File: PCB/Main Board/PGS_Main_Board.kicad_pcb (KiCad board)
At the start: 4 copper layers, 109.9 x 60.8 mm, 132 parts, among them J1 SM02B-SURS-TF_LF__SN_, J2 SM02B-SURS-TF_LF__SN_, J3 Molex 505110-0892, J5 Molex 505110-0892, J6 Molex 505110-0492, J7 Molex 505110-0492, J8 Conn_01x04_Pin, J9 Molex 505110-1792, Q1 MMBT2222A, Q2 MMBT2222A, SW1 TS-1187A-C-A-B, SW10 SW_Push, SW11 SW_Push, SW12 SW_Push, SW13 SW_Push, SW14 EVQ-P0E07K, SW15 1TS026A-1000-0550, SW16 TS-1187A-C-A-B, SW2 TS-1187A-C-A-B, SW3 TS-1187A-C-A-B, SW4 TS-1187A-C-A-B, SW5 SW_Push, SW6 SW_Push, SW7 SW_Push, SW8 SW_Push, SW9 EVQ-P0E07K, U1 RP2040, U2 TPS630001RCR, U3 GD25Q80EEIGR, U4 ST_LSM6, U5 ST_LSM6, Y1 ABM8-272-T3

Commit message: PCB Routing
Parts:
- C1, C15, C16, C17, C2, C20, C24, C25, C26, C27, C4, C5, R1, R11, S1, U2, Y1: moved to B.Cu
- moved R11 94.8 mm to (65.5, 39.7), turned to 45 degrees
- moved C16 90.2 mm to (65.5, 38.3), turned to -135 degrees
- moved C4 86.5 mm to (68.8, 32.6), turned to -135 degrees
- moved D13 85.7 mm to (56.6, 43.4)
- moved D14 84.7 mm to (56.6, 46.2)
- moved C5 84.1 mm to (65.3, 30.8), turned to -135 degrees
- moved R1 78.4 mm to (68.0, 22.2), turned to 45 degrees
- moved C24 76.7 mm to (57.0, 14.9), turned to 180 degrees
- moved C26 73.3 mm to (58.5, 14.9)
- moved R24 72.3 mm to (105.4, 30.2)
- moved D15 72.2 mm to (92.3, 38.1), turned to 180 degrees
- moved C20 67.7 mm to (68.9, 20.8), turned to -45 degrees
- moved S1 66.2 mm to (76.6, 22.7), turned to 180 degrees
- moved D16 65.4 mm to (92.3, 35.3), turned to 180 degrees
- moved C27 60.3 mm to (84.1, 14.9)
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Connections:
- net Net-(U1-USB_DM) renamed DI-
- net Net-(U1-USB_DP) renamed DI+
- J9 pad 13: D+ -> VBUS_SYS
- J9 pad 14: D- -> VBUS_SYS
- J9 pad 15: VBUS_SYS -> D+
- J9 pad 16: VBUS_SYS -> D-
- R21 pad 1: Net-(U1-GPIO16) -> unconnected-(R21-Pad1)
- R22 pad 1: Net-(U1-GPIO17) -> unconnected-(R22-Pad1)
- R24 pad 1: Net-(U1-GPIO19) -> Net-(U1-GPIO25)
- SW10 pad 2: Net-(D15A-A) -> Net-(D16B-A)
- SW11 pad 2: Net-(D15B-A) -> Net-(D16A-A)
- SW12 pad 2: Net-(D15C-A) -> Net-(D15A-A)
- SW13 pad 2: Net-(D16A-A) -> Net-(D15B-A)
- SW5 pad 2: Net-(D13A-A) -> Net-(D14A-A)
- SW6 pad 2: Net-(D13B-A) -> Net-(D13C-A)
- SW7 pad 2: Net-(D13C-A) -> Net-(D14B-A)
- SW8 pad 2: Net-(D14A-A) -> Net-(D13B-A)
- U1 pad 27: Net-(U1-GPIO16) -> I2C0_SDA
- U1 pad 28: Net-(U1-GPIO17) -> I2C0_SCL
- U1 pad 30: Net-(U1-GPIO19) -> unconnected-(U1-GPIO19-Pad30)
- U1 pad 31: ADC_ADDR_0 -> unconnected-(U1-GPIO20-Pad31)
- U1 pad 32: ADC_ADDR_1 -> unconnected-(U1-GPIO21-Pad32)
- U1 pad 36: I2C0_SDA -> unconnected-(U1-GPIO24-Pad36)
- U1 pad 37: I2C0_SCL -> Net-(U1-GPIO25)
- U1 pad 38: unconnected-(U1-GPIO26_ADC0-Pad38) -> ADC_ADDR_0
- U1 pad 39: unconnected-(U1-GPIO27_ADC1-Pad39) -> ADC_ADDR_1
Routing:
- net +3V3: track 0.00 -> 74.5 mm, vias 0 -> 31
- net GND: track 0.00 -> 65.3 mm, vias 0 -> 24
- net Net-(D15C-A): track 0.00 -> 53.9 mm, vias 0 -> 1
- net Net-(D13B-A): track 0.00 -> 53.6 mm
- net Net-(RGB3-DOUT): track 0.00 -> 47.8 mm
- net Net-(D16A-A): track 0.00 -> 41.1 mm, vias 0 -> 1
- net Net-(D13A-A): track 0.00 -> 38.7 mm
- net I2C0_SDA: track 0.00 -> 35.8 mm, vias 0 -> 3
- net BAT_LVL: track 0.00 -> 35.1 mm
- net I2C0_SCL: track 0.00 -> 34.4 mm, vias 0 -> 3
- net Net-(RGB5-DOUT): track 0.00 -> 33.6 mm
- net Net-(D15B-A): track 0.00 -> 31.9 mm, vias 0 -> 1
- net WL_CS: track 0.00 -> 29.7 mm
- net WL_CLK: track 0.00 -> 28.9 mm
- net I2C1_SCL: track 0.00 -> 28.6 mm, vias 0 -> 1
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
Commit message: Routing update
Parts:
- removed C15, C17: 10uF, Capacitor_SMD:C_0805_2012Metric
- removed C16: 100nF, Capacitor_SMD:C_0201_0603Metric
- removed D7: CUS08F30,H3F, Diode_SMD:D_SOD-323_HandSoldering
- removed L1: 1.3A 2.2uH ±20% 80mΩ, Inductor_SMD:L_1008_2520Metric
- removed R23: 100R, Resistor_SMD:R_0201_0603Metric
- removed TP1, TP2, TP3, TP4: TestPoint, TestPoint:TestPoint_Pad_2.0x2.0mm
- removed TP5: TestPoint, TestPoint:TestPoint_Pad_D1.5mm
- removed U2: TPS630001RCR, hhl:VREG_V62_16624-01YE
- R18, R19, R20, R21, R22: moved to B.Cu
- moved R9 138.3 mm to (28.1, 66.2), turned to 180 degrees
- moved T1 135.2 mm to (26.9, 58.1), turned to -90 degrees
- moved T2 134.0 mm to (24.8, 58.1), turned to -90 degrees
- moved C12 131.4 mm to (32.7, 63.7)
- moved C11 124.6 mm to (27.9, 68.5)
- moved R5 120.3 mm to (32.6, 58.1)
- moved C13 118.0 mm to (115.7, 65.2), turned to 90 degrees
- moved R10 117.8 mm to (113.1, 66.2)
- moved R7 117.1 mm to (33.8, 58.6), turned to -90 degrees
- moved C9 116.9 mm to (32.6, 58.9), turned to 180 degrees
- moved C14 113.5 mm to (109.7, 63.4), turned to 180 degrees
- moved T3 103.7 mm to (118.9, 58.4)
- moved T4 102.7 mm to (118.9, 60.5)
- moved Q1 100.1 mm to (32.8, 61.3), turned to -90 degrees
- moved R6 99.9 mm to (112.6, 56.6), turned to 90 degrees
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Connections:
- D11 pad 2: Net-(D11B-A) -> T_ZR_OUT
- D12 pad 1: T_ZR_OUT -> Net-(D12A-A)
- D8 pad 2: Net-(D8B-A) -> T_ZL_OUT
- D8 pad 5: B -> D
- D8 pad 6: A -> E
- D9 pad 1: T_ZL_OUT -> STICK_L_BTN_OUT
- D9 pad 2: STICK_L_BTN_OUT -> Net-(D9B-A)
- D9 pad 5: E -> A
- D9 pad 6: D -> B
- J3 pad 7: G -> F
- J5 pad 7: F -> G
- J6 pad 1: F -> G
- J6 pad 4: F -> G
- J7 pad 1: G -> F
- J7 pad 4: G -> F
- J9 pad 13: VBUS_SYS -> +3V3
- J9 pad 14: VBUS_SYS -> +3V3
- R11 pad 1: VBUS_SYS -> Net-(U1-GPIO10)
- R11 pad 2: Net-(U2-EN) -> A
- R15 pad 1: Net-(U1-GPIO10) -> unconnected-(R15-Pad1)
- R16 pad 1: Net-(U1-GPIO11) -> unconnected-(R16-Pad1)
- R17 pad 1: Net-(U1-GPIO12) -> unconnected-(R17-Pad1)
- R18 pad 1: Net-(U1-GPIO13) -> Net-(U1-GPIO15)
- R20 pad 1: Net-(U1-GPIO15) -> Net-(U1-GPIO13)
- R21 pad 1: unconnected-(R21-Pad1) -> Net-(U1-GPIO12)
- R22 pad 1: unconnected-(R22-Pad1) -> Net-(U1-GPIO11)
- S1 pad 2: LY -> STICK_R_X_OUT
- S1 pad 4: LX -> STICK_R_Y_OUT
- S1 pad 7: RX -> STICK_L_X_OUT
- S1 pad 9: RY -> STICK_L_Y_OUT
- SW1 pad A: F -> G
- SW1 pad B: F -> G
- SW2 pad A: F -> G
- SW2 pad B: F -> G
- SW2 pad C: Net-(D8B-A) -> Net-(D9B-A)
- SW2 pad D: Net-(D8B-A) -> Net-(D9B-A)
- SW3 pad A: G -> F
- SW3 pad B: G -> F
- SW4 pad A: G -> F
- SW4 pad B: G -> F
- SW4 pad C: Net-(D11B-A) -> Net-(D12A-A)
- SW4 pad D: Net-(D11B-A) -> Net-(D12A-A)
- U1 pad 29: Net-(U1-GPIO18) -> unconnected-(U1-GPIO18-Pad29)
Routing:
- net F: track 0.00 -> 109.0 mm, vias 0 -> 5
- net H: track 0.00 -> 82.5 mm, vias 0 -> 8
- net STICK_L_Y_OUT: track 0.00 -> 52.6 mm, vias 0 -> 2
- net STICK_L_X_OUT: track 0.00 -> 51.7 mm, vias 0 -> 2
- net D: track 0.00 -> 35.2 mm, vias 0 -> 2
- net E: track 0.00 -> 34.9 mm, vias 0 -> 2
- net C: track 0.00 -> 32.9 mm, vias 0 -> 2
- net B: track 0.00 -> 32.2 mm, vias 0 -> 2
- net A: track 0.00 -> 29.0 mm, vias 0 -> 2
- net LRA_R+: track 0.00 -> 22.5 mm, vias 0 -> 1
- net STICK_R_BTN_OUT: track 0.00 -> 21.7 mm, vias 0 -> 1
- net VBUS_SYS: track 20.3 -> 0.00 mm
- net LRA_L+: track 0.00 -> 19.9 mm, vias 0 -> 1
- net LRA_R-: track 0.00 -> 18.5 mm, vias 0 -> 1
- net STICK_L_BTN_OUT: track 0.00 -> 17.1 mm, vias 0 -> 1
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
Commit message: More Routing
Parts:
- C21, R15, R16, R17: moved to B.Cu
- moved R15 67.3 mm to (72.2, 19.7), turned to 45 degrees
- moved R17 66.1 mm to (73.6, 22.5), turned to 90 degrees
- moved R16 65.4 mm to (71.6, 19.1), turned to 45 degrees
- moved C21 65.0 mm to (72.9, 21.2), turned to -45 degrees
- moved R24 1.63 mm to (105.3, 28.6)
- moved D11 0.34 mm to (84.5, 31.8)
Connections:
- J3 pad 7: F -> G
- J5 pad 7: G -> F
- J6 pad 1: G -> F
- J6 pad 4: G -> F
- J7 pad 1: F -> G
- J7 pad 4: F -> G
- R15 pad 1: unconnected-(R15-Pad1) -> Net-(U1-GPIO19)
- R16 pad 1: unconnected-(R16-Pad1) -> Net-(U1-GPIO18)
- R17 pad 1: unconnected-(R17-Pad1) -> Net-(U1-GPIO22)
- S1 pad 2: STICK_R_X_OUT -> STICK_R_Y_OUT
- S1 pad 4: STICK_R_Y_OUT -> STICK_R_X_OUT
- SW1 pad A: G -> F
- SW1 pad B: G -> F
- SW2 pad A: G -> F
- SW2 pad B: G -> F
- SW3 pad A: F -> G
- SW3 pad B: F -> G
- SW4 pad A: F -> G
- SW4 pad B: F -> G
- U1 pad 29: unconnected-(U1-GPIO18-Pad29) -> Net-(U1-GPIO18)
- U1 pad 30: unconnected-(U1-GPIO19-Pad30) -> Net-(U1-GPIO19)
- U1 pad 31: unconnected-(U1-GPIO20-Pad31) -> LRA_L
- U1 pad 32: unconnected-(U1-GPIO21-Pad32) -> LRA_R
- U1 pad 34: LRA_L -> Net-(U1-GPIO22)
- U1 pad 35: LRA_R -> unconnected-(U1-GPIO23-Pad35)
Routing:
- net I: track 0.00 -> 122.4 mm, vias 0 -> 5
- net LRA_R: track 1.59 -> 95.3 mm, vias 0 -> 7
- net LRA_L: track 1.71 -> 74.9 mm, vias 0 -> 3
- net H: track 82.5 -> 149.4 mm, vias 8 -> 9
- net STICK_R_Y_OUT: track 1.07 -> 56.2 mm, vias 1 -> 4
- net STICK_R_X_OUT: track 1.40 -> 53.7 mm, vias 1 -> 4
- net G: track 0.00 -> 52.1 mm, vias 0 -> 3
- net F: track 109.0 -> 57.8 mm, vias 5 -> 3
- net Net-(U1-GPIO25): track 0.00 -> 47.4 mm, vias 0 -> 3
- net Net-(D14A-A): track 19.6 -> 12.9 mm
- net +3V3: track 84.1 -> 88.5 mm, vias 33 -> 34
- net Net-(U1-GPIO18): track 0.00 -> 3.57 mm
- net Net-(U1-GPIO19): track 0.00 -> 3.43 mm
- net I2C0_SCL: track 35.0 -> 38.0 mm
- net GND: track 71.4 -> 73.9 mm, vias 24 -> 26
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
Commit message: Routing/Labelling
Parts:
- removed C19: 100nF, Capacitor_SMD:C_0201_0603Metric
- C18, C22, C7, C8: moved to B.Cu
- C28: footprint Capacitor_SMD:C_0402_1005Metric -> Capacitor_SMD:C_0201_0603Metric; moved to B.Cu
- moved C18 76.5 mm to (76.0, 28.9), turned to 180 degrees
- moved C7 73.5 mm to (77.8, 26.6), turned to 180 degrees
- moved C8 72.5 mm to (77.8, 27.4), turned to 180 degrees
- moved C28 70.7 mm to (77.9, 25.4)
- moved C22 68.7 mm to (77.8, 28.2), turned to 180 degrees
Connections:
- D11 pad 5: B -> D
- D11 pad 6: A -> E
- D12 pad 5: E -> A
- D12 pad 6: D -> B
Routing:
- net C: track 32.9 -> 78.3 mm, vias 2 -> 3
- net D: track 35.2 -> 78.8 mm, vias 2 -> 3
- net E: track 34.9 -> 78.2 mm, vias 2 -> 3
- net B: track 32.2 -> 73.5 mm, vias 2 -> 3
- net A: track 29.0 -> 69.0 mm, vias 2 -> 3
- net STICK_R_RGB_OUT: track 5.36 -> 42.3 mm, vias 2 -> 1
- net G: track 52.1 -> 64.3 mm
- net SWD: track 1.39 -> 12.0 mm
- net SWCLK: track 1.71 -> 12.3 mm
- net +1V1: track 5.67 -> 15.6 mm
- net GND: track 73.9 -> 82.1 mm, vias 26 -> 51
- net +3V3: track 88.5 -> 94.0 mm, vias 34 -> 35
- net BAT_LVL: track 34.6 -> 37.0 mm
- net F: track 57.8 -> 58.7 mm
- net H: track 149.4 -> 148.6 mm
- added copper zone on B.Cu, net +3V3
- added copper zone on In2.Cu, net +3V3
- added copper zone on B.Cu, net GND
- added copper zone on F.Cu, net GND
- added copper zone on In1.Cu, net GND
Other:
- board text added: "3.3v"
- board text added: "A"
- board text added: "B"
- board text added: "BOOTLOADER"
- board text added: "CAPTURE"
- board text added: "COMMS+POWER"
- board text added: "CRYSTAL"
- board text added: "DEBUG"
- board text added: "FLASH"
- board text added: "HAPTICS L"
- board text added: "HAPTICS R"
- board text added: "HOME"
- board text added: "Hand Held Legend, LLC Designed By Mitch"
- board text added: "I2C EXT"
- board text added: "IMU 1"
- board text added: "IMU 2"
- board text added: "L/ZL"
- board text added: "LB"
- board text added: "LEFT JOYSTICK"
- board text added: "MINUS"
- board text added: "MUX"
- board text added: "PLUS"
- board text added: "POWER"
- board text added: "ProGCC 4.0 Main Board"
- board text added: "R/ZR"
- board text added: "RB"
- board text added: "RIGHT JOYSTICK"
- board text added: "RP2040"
- board text added: "X"
- board text added: "Y"
- board text added: "gnd"
- board text added: "swclk"
- board text added: "swd"

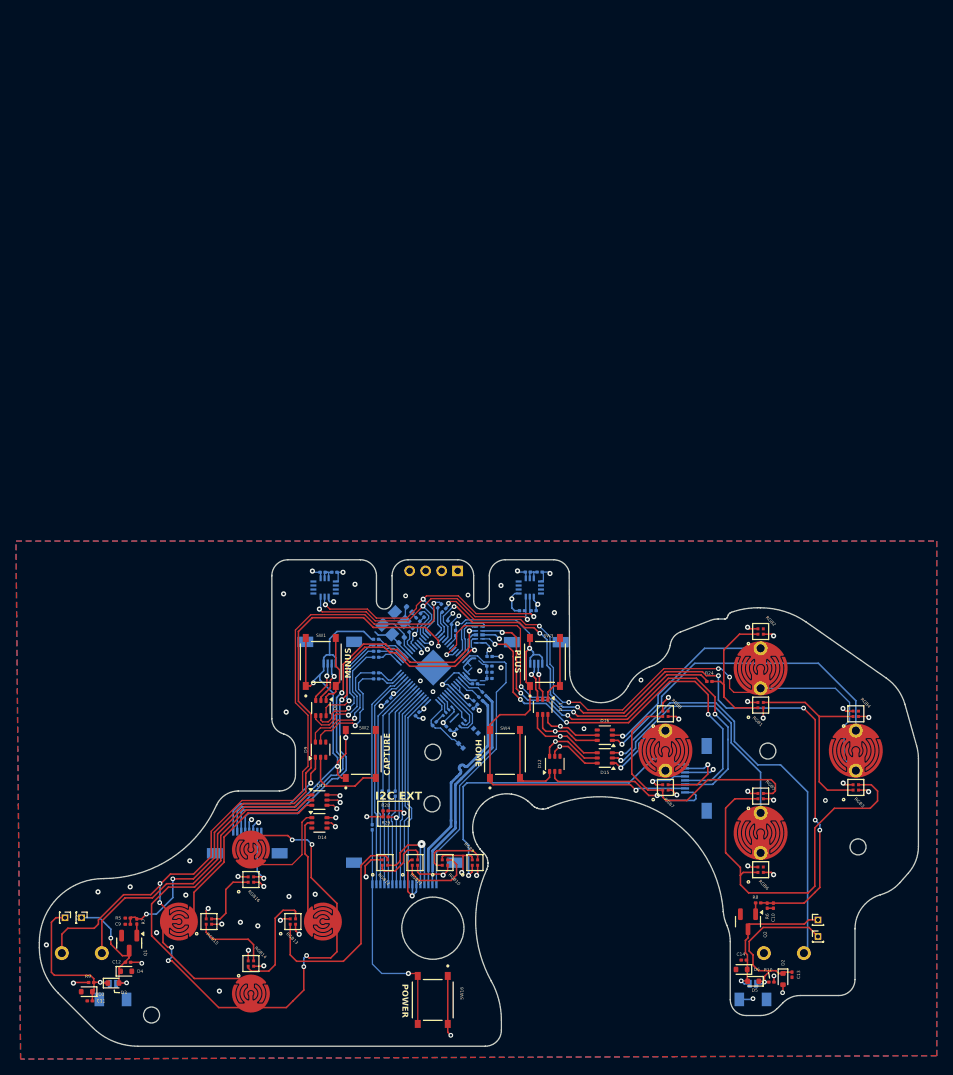
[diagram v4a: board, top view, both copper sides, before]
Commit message: Board Pos Fixes
- Fix RGB Resistor position
- Move input matrix diode arrays
- Move conflicting LRA driver components
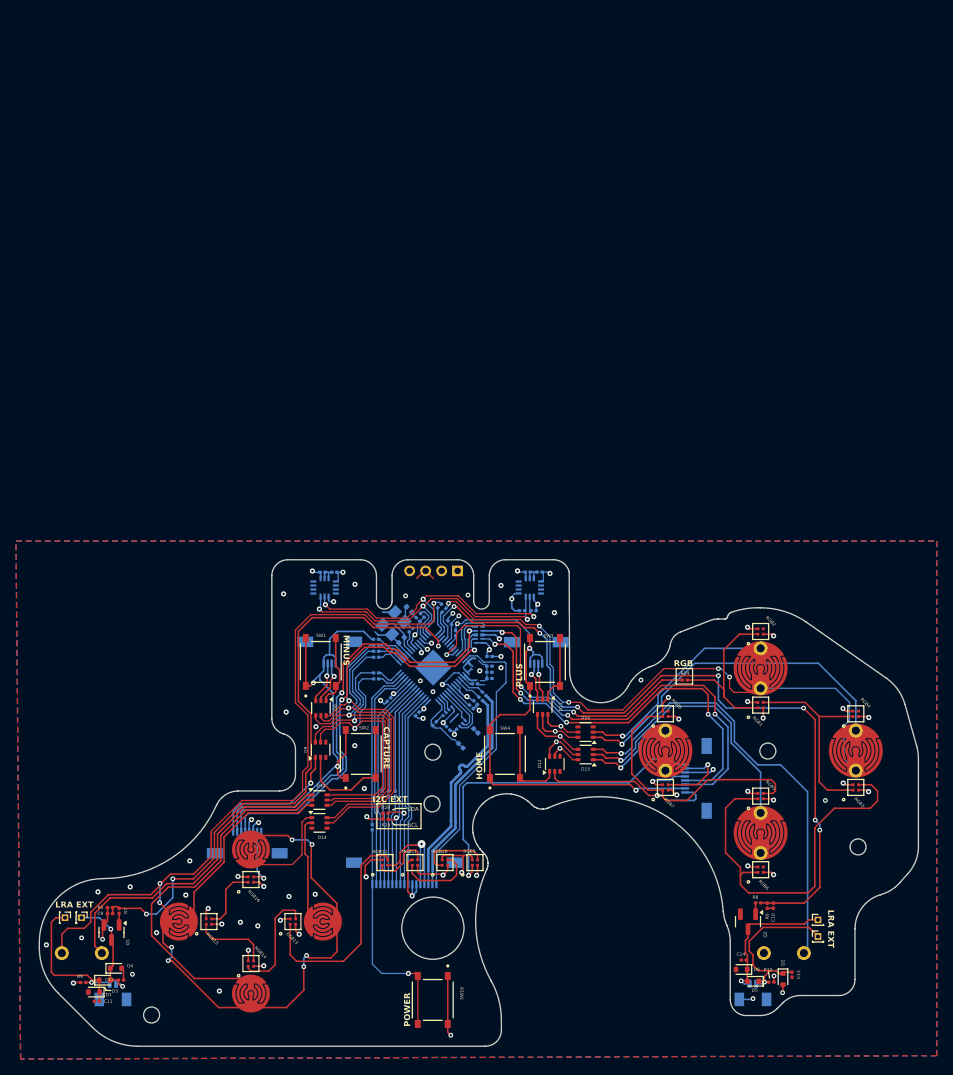
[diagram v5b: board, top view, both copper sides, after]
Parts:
- moved R24 3.08 mm to (102.3, 28.4)
- moved R7 2.58 mm to (31.6, 57.2)
- moved Q1 2.58 mm to (30.6, 60.0)
- moved C9 2.58 mm to (30.4, 57.6)
- moved R5 2.58 mm to (30.4, 56.8)
- moved D15 2.44 mm to (89.9, 37.7)
- moved D16 2.43 mm to (89.9, 34.9)
- moved C12 2.39 mm to (31.8, 65.9)
- moved D4 1.33 mm to (31.2, 64.4)
- moved D3 1.13 mm to (29.8, 65.9)
- moved R9 1.00 mm to (27.1, 66.2)
- moved D1 0.90 mm to (28.4, 67.4)
- moved C11 0.90 mm to (28.8, 68.5)
- moved R29 0.28 mm to (64.9, 45.0)
- moved R28 0.28 mm to (64.9, 45.8)
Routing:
- net GND: track 82.1 -> 91.5 mm, vias 51 -> 55
- net Net-(U1-GPIO25): track 47.6 -> 43.9 mm
- net RGB_OUT: track 18.9 -> 21.7 mm
- net Net-(D15C-A): track 53.9 -> 56.5 mm
- net Net-(D15B-A): track 31.9 -> 34.5 mm
- net Net-(D15A-A): track 9.27 -> 11.8 mm
- net Net-(D16B-A): track 23.7 -> 26.3 mm
- net Net-(D16A-A): track 41.1 -> 43.7 mm
- net LRA_L: track 74.9 -> 77.1 mm
- net LRA_L-: track 16.1 -> 14.0 mm
- net A: track 69.0 -> 71.0 mm, vias 3 -> 2
- net Net-(D13A-A): track 38.6 -> 40.5 mm
- net C: track 78.3 -> 80.0 mm, vias 3 -> 2
- net LRA_L+: track 19.7 -> 20.9 mm
- net +3V3: track 94.0 -> 94.8 mm
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- added copper zone on In1.Cu, net +3V3
- added copper zone on In2.Cu, net GND
- removed copper zone on In2.Cu, net +3V3
- removed copper zone on In1.Cu, net GND
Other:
- board text added: "LRA EXT"
- board text added: "RGB"
- board text added: "SCL"
- board text added: "SDA"

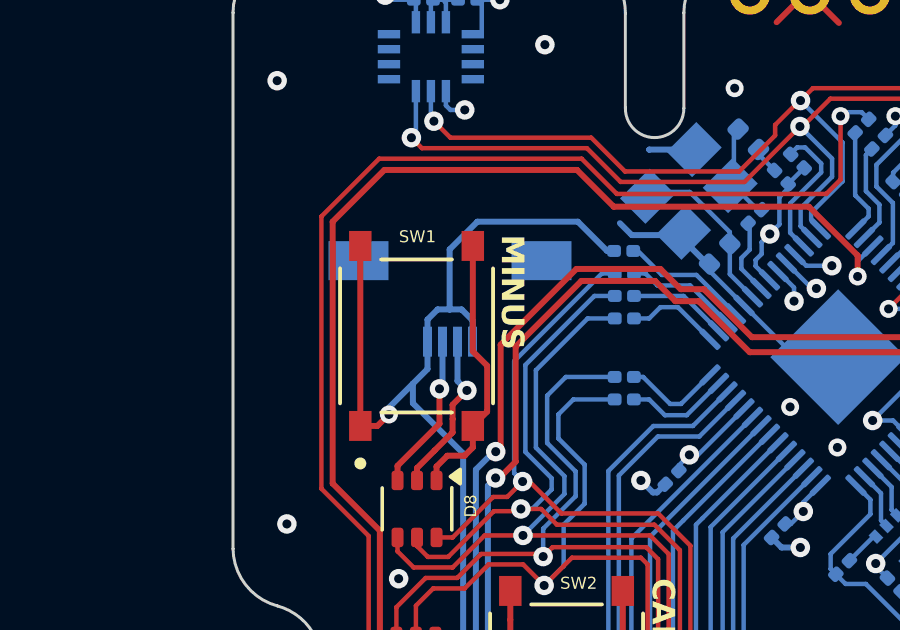
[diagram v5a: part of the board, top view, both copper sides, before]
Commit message: More Routing
- Stick Module Done
- BT Comms + Power Done
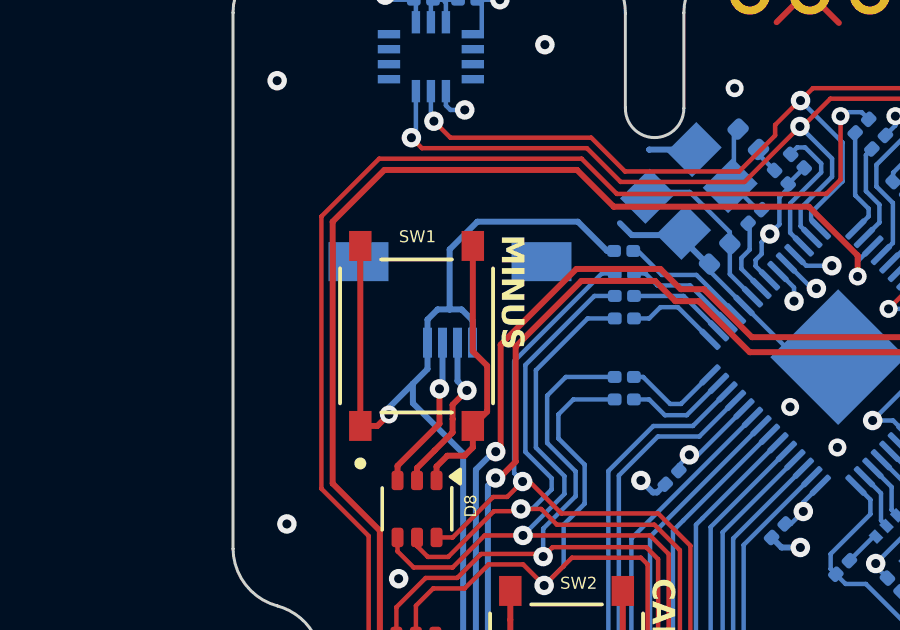
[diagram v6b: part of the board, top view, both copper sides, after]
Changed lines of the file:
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@@
 	(footprint "hhl:5051100492"
 		(layer "B.Cu")
-		(at 57.88679 24.098948)
+		(at 57.88679 24.132331)
 		(descr "505110-0492-1")
 		(tags "Connector")
@@
 	)
 	(segment
-		(start 57.63679 26.323948)
+		(start 57.63679 26.357331)
 		(end 57.63679 27.796052)
 		(width 0.2)
@@
 	)
 	(segment
-		(start 58.13679 27.63679)
-		(end 58.13679 26.323948)
+		(start 58.45 27.95)
+		(end 58.13679 27.63679)
 		(width 0.2)
 		(layer "B.Cu")
@@
 	)
 	(segment
-		(start 58.45 27.95)
-		(end 58.13679 27.63679)
+		(start 58.13679 27.63679)
+		(end 58.13679 26.357331)
 		(width 0.2)
 		(layer "B.Cu")
@@
 	)
 	(segment
-		(start 57.875 25.25)
-		(end 58.275 25.25)
-		(width 0.2)
-		(layer "B.Cu")
-		(net 62)
-	)
-	(segment
 		(start 56.65 28.375)
 		(end 58.325 30.05)
@@
 	)
 	(segment
+		(start 58.275 25.25)
+		(end 58.63679 25.61179)
+		(width 0.2)
+		(layer "B.Cu")
+		(net 62)
+	)
+	(segment
 		(start 55.85 28.525)
 		(end 55.85 28.75)
@@
 	)
 	(segment
-		(start 58.8 22.325)
-		(end 62.15 22.325)
+		(start 58.63679 25.61179)
+		(end 58.63679 26.357331)
 		(width 0.2)
 		(layer "B.Cu")
@@
 	)
 	(segment
-		(start 58.275 25.25)
-		(end 58.63679 25.61179)
+		(start 58.8 22.325)
+		(end 62.15 22.325)
 		(width 0.2)
 		(layer "B.Cu")
@@
 	)
 	(segment
+		(start 57.875 25.25)
+		(end 58.275 25.25)
+		(width 0.2)
+		(layer "B.Cu")
+		(net 62)
+	)
+	(segment
 		(start 58.325 37.55)
 		(end 58.874258 38.099258)
@@
 		(width 0.2)
 		(layer "B.Cu")
-		(net 62)
-	)
-	(segment
-		(start 58.63679 25.61179)
-		(end 58.63679 26.323948)
-		(width 0.2)
-		(layer "B.Cu")
